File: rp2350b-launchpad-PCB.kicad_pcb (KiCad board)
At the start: 2 copper layers, 58.4 x 83.8 mm, 127 parts, among them J1 Target Isolation Jumpers, J10 PWR Header, J11 LP Extension Heder, J12 LP Header right, J13 PWR Header, J2 Jumper, J3 LiPo 3,7V Batt., J4 Jumper, J5 DBG_PRGM, J6 UART_DBG, J7 DGB Exp. Header, J8 Jumper, J9 LP Header left, SW1 Switch_SP3T, SW2 RESET, SW3 BOOT, U1 MCP73831, U10 WS2812B-2020, U11 WS2812B-2020, U12 WS2812B-2020, U13 WS2812B-2020, U14 WS2812B-2020, U15 WS2812B-2020, U16 WS2812B-2020, U2 XC9142B50C, U3 XC6220B33, U4 25Q32, U5 RP2040, U6 25Q64, U7 APS6404L-3SQR, U8 RP2350_80QFN, U9 WS2812B-2020, Y1 12MHz, Y2 12MHz

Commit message: Footprint cleanup.
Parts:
- U5: footprint rp2350b-launchpad-PCB:QFN40P700X700X90-57N -> Package_DFN_QFN:QFN-56-1EP_7x7mm_P0.4mm_EP3.2x3.2mm_ThermalVias
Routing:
- net GND_DBG: vias 54 -> 52

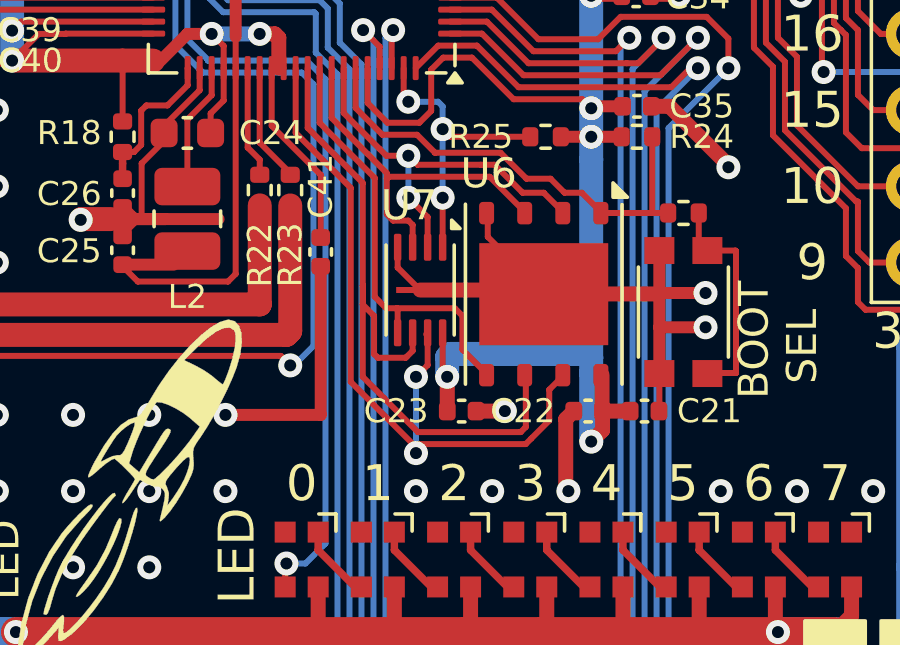
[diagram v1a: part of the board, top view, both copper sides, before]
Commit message: Fixed gerber file names.
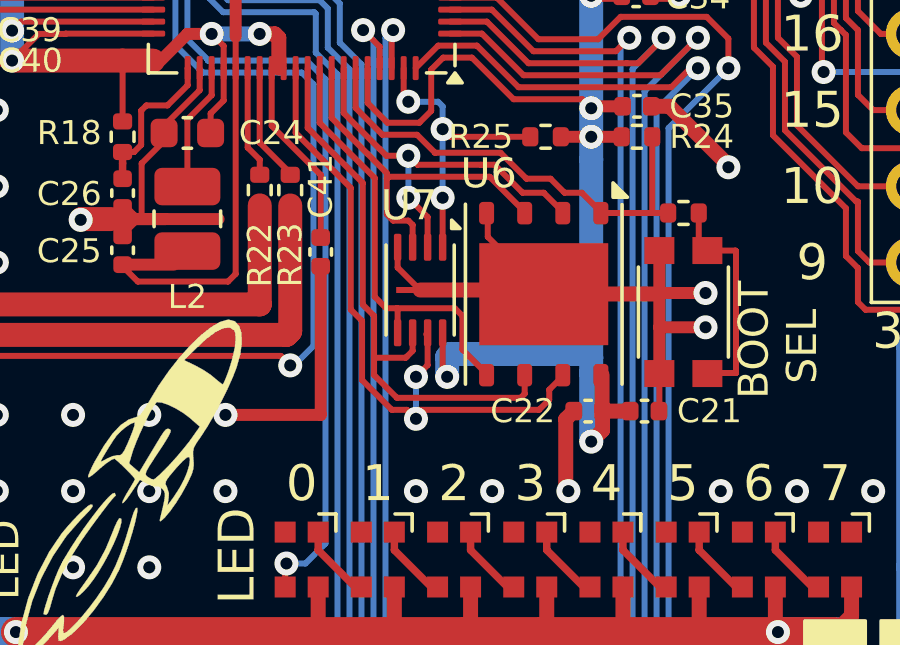
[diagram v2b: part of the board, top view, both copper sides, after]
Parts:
- removed C23: 100nF, Capacitor_SMD:C_0402_1005Metric
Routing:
- net /Target/SCLK: track 23.5 -> 19.1 mm
- net /Target/SD3: track 25.5 -> 22.6 mm
- net +3V3: track 318.8 -> 317.6 mm
- net GND: track 94.1 -> 93.1 mm, vias 98 -> 97
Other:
- rule pad_to_mask_clearance: 0.051 -> 0

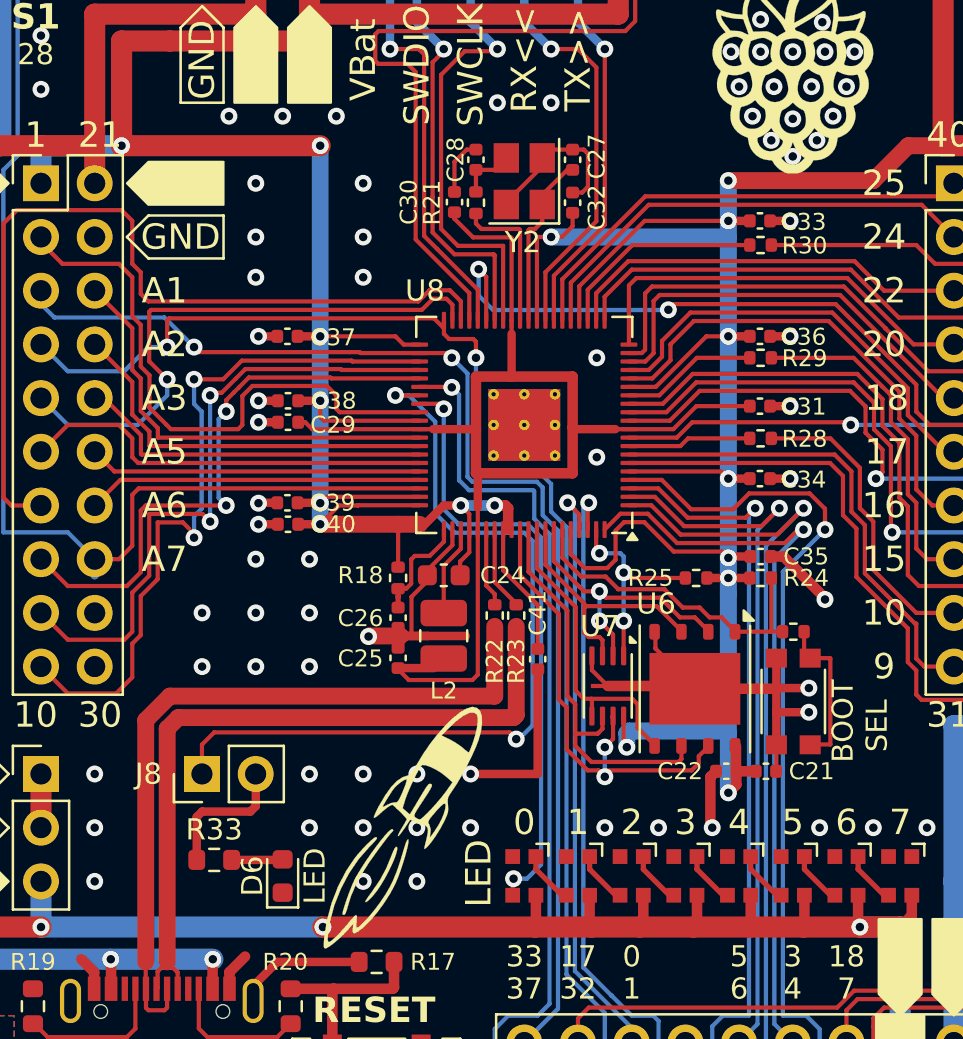
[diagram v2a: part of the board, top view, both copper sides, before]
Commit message: Renumbering parts on target.
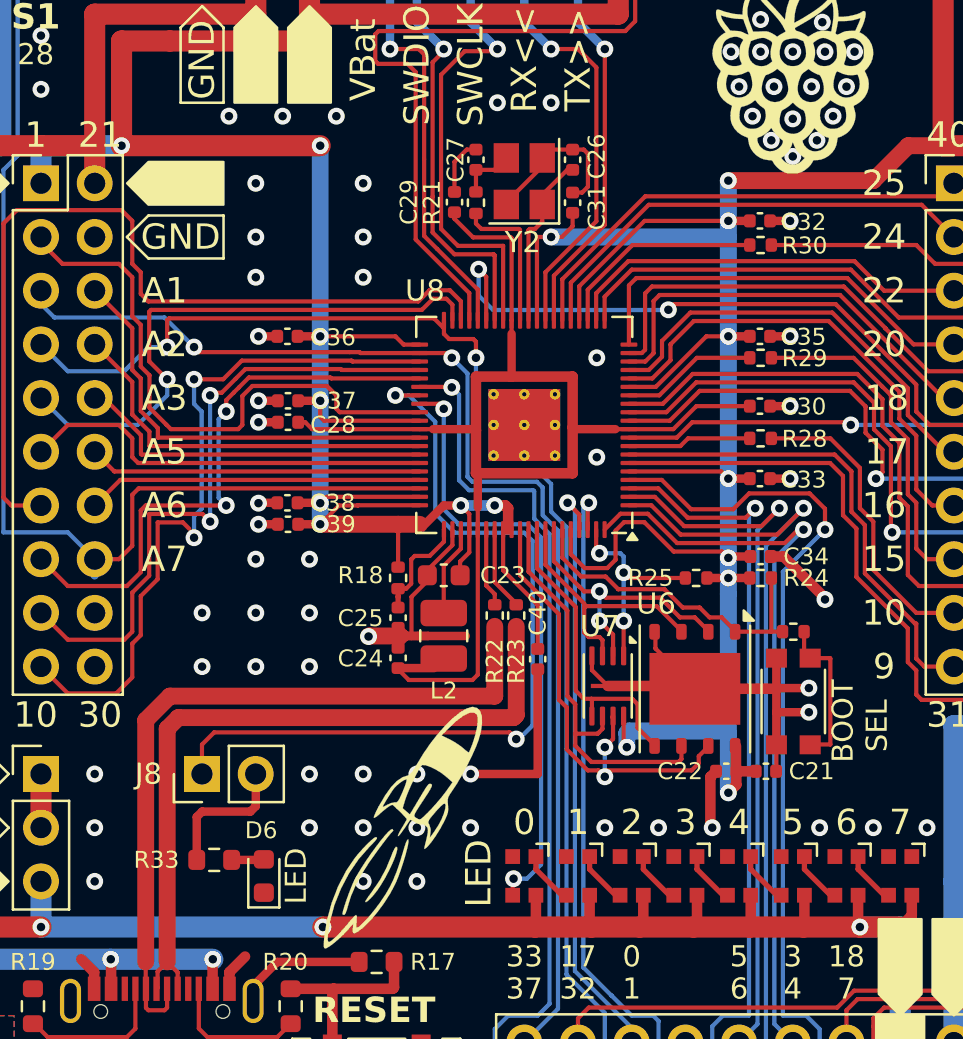
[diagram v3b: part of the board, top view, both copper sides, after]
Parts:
- moved D6 0.89 mm to (127.4, 139.4)
- renumbered C24 to C23, C25 to C24, C26 to C25, C27 to C26, C28 to C27, C29 to C28, C30 to C29, C31 to C30, C32 to C31, C33 to C32, C34 to C33, C35 to C34, C36 to C35, C37 to C36, C38 to C37, C39 to C38, C40 to C39, C41 to C40
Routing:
- net Net-(D6-A): track 2.49 -> 1.53 mm
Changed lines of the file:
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@@
 	(net 10 "Net-(U8-VREG_AVDD)")
 	(net 11 "Net-(U8-XIN)")
-	(net 12 "Net-(C28-Pad2)")
+	(net 12 "Net-(C27-Pad2)")
 	(net 13 "+1V1")
 	(net 14 "Net-(D1-K)")
@@
 		(descr "Capacitor SMD 0603 (1608 Metric), square (rectangular) end terminal, IPC_7351 nominal, (Body size source: IPC-SM-782 page 76, https://www.pcb-3d.com/wordpress/wp-content/uploads/ipc-sm-782a_amendment_1_and_2.pdf), generated with kicad-footprint-generator")
 		(tags "capacitor")
-		(property "Reference" "C24"
+		(property "Reference" "C23"
 			(at 2.794 0 0)
 			(layer "F.SilkS")
@@
 		(descr "Capacitor SMD 0402 (1005 Metric), square (rectangular) end terminal, IPC_7351 nominal, (Body size source: IPC-SM-782 page 76, https://www.pcb-3d.com/wordpress/wp-content/uploads/ipc-sm-782a_amendment_1_and_2.pdf), generated with kicad-footprint-generator")
 		(tags "capacitor")
-		(property "Reference" "C34"
+		(property "Reference" "C33"
 			(at 2.06 0.0508 0)
 			(layer "F.SilkS")
@@
 		(descr "Capacitor SMD 0402 (1005 Metric), square (rectangular) end terminal, IPC_7351 nominal, (Body size source: IPC-SM-782 page 76, https://www.pcb-3d.com/wordpress/wp-content/uploads/ipc-sm-782a_amendment_1_and_2.pdf), generated with kicad-footprint-generator")
 		(tags "capacitor")
-		(property "Reference" "C37"
+		(property "Reference" "C36"
 			(at -2.1564 -0.0508 180)
 			(layer "F.SilkS")
@@
 		(descr "Capacitor SMD 0402 (1005 Metric), square (rectangular) end terminal, IPC_7351 nominal, (Body size source: IPC-SM-782 page 76, https://www.pcb-3d.com/wordpress/wp-content/uploads/ipc-sm-782a_amendment_1_and_2.pdf), generated with kicad-footprint-generator")
 		(tags "capacitor")
-		(property "Reference" "C39"
+		(property "Reference" "C38"
 			(at -2.131 0 180)
 			(layer "F.SilkS")
@@
 		(descr "Capacitor SMD 0402 (1005 Metric), square (rectangular) end terminal, IPC_7351 nominal, (Body size source: IPC-SM-782 page 76, https://www.pcb-3d.com/wordpress/wp-content/uploads/ipc-sm-782a_amendment_1_and_2.pdf), generated with kicad-footprint-generator")
 		(tags "capacitor")
-		(property "Reference" "C26"
+		(property "Reference" "C25"
 			(at -1.877 1.778 0)
 			(layer "F.SilkS")
@@
 		(descr "Capacitor SMD 0402 (1005 Metric), square (rectangular) end terminal, IPC_7351 nominal, (Body size source: IPC-SM-782 page 76, https://www.pcb-3d.com/wordpress/wp-content/uploads/ipc-sm-782a_amendment_1_and_2.pdf), generated with kicad-footprint-generator")
 		(tags "capacitor")
-		(property "Reference" "C30"
+		(property "Reference" "C29"
 			(at 0 -2.159 90)
 			(layer "F.SilkS")
@@
 		(descr "Capacitor SMD 0402 (1005 Metric), square (rectangular) end terminal, IPC_7351 nominal, (Body size source: IPC-SM-782 page 76, https://www.pcb-3d.com/wordpress/wp-content/uploads/ipc-sm-782a_amendment_1_and_2.pdf), generated with kicad-footprint-generator")
 		(tags "capacitor")
-		(property "Reference" "C31"
+		(property "Reference" "C30"
 			(at 2.06 0.0254 0)
 			(layer "F.SilkS")
@@
 		(descr "Capacitor SMD 0402 (1005 Metric), square (rectangular) end terminal, IPC_7351 nominal, (Body size source: IPC-SM-782 page 76, https://www.pcb-3d.com/wordpress/wp-content/uploads/ipc-sm-782a_amendment_1_and_2.pdf), generated with kicad-footprint-generator")
 		(tags "capacitor")
-		(property "Reference" "C28"
+		(property "Reference" "C27"
 			(at 0 0.962 90)
 			(layer "F.SilkS")
@@
 			(layers "F.Cu" "F.Paste" "F.Mask")
 			(roundrect_rratio 0.25)
-			(net 12 "Net-(C28-Pad2)")
+			(net 12 "Net-(C27-Pad2)")
 			(pintype "passive")
 		)
@@
 		(descr "Capacitor SMD 0402 (1005 Metric), square (rectangular) end terminal, IPC_7351 nominal, (Body size source: IPC-SM-782 page 76, https://www.pcb-3d.com/wordpress/wp-content/uploads/ipc-sm-782a_amendment_1_and_2.pdf), generated with kicad-footprint-generator")
 		(tags "capacitor")
-		(property "Reference" "C41"
+		(property "Reference" "C40"
 			(at -2.187 0 90)
 			(layer "F.SilkS")
@@
 		(tags "resistor")
 		(property "Reference" "R33"
-			(at 0 -1.43 0)
+			(at -2.731 0 0)
 			(layer "F.SilkS")
 			(effects
 				(font
-					(size 1 1)
+					(size 0.8 0.8)
 					(thickness 0.15)
 				)
@@
 			(layers "F.Cu" "F.Paste" "F.Mask")
 			(roundrect_rratio 0.25)
-			(net 12 "Net-(C28-Pad2)")
+			(net 12 "Net-(C27-Pad2)")
 			(pintype "passive")
 		)
@@
 		(descr "Capacitor SMD 0402 (1005 Metric), square (rectangular) end terminal, IPC_7351 nominal, (Body size source: IPC-SM-782 page 76, https://www.pcb-3d.com/wordpress/wp-content/uploads/ipc-sm-782a_amendment_1_and_2.pdf), generated with kicad-footprint-generator")
 		(tags "capacitor")
-		(property "Reference" "C38"
+		(property "Reference" "C37"
 			(at -2.159 0 180)
 			(layer "F.SilkS")
@@
 		(descr "Capacitor SMD 0402 (1005 Metric), square (rectangular) end terminal, IPC_7351 nominal, (Body size source: IPC-SM-782 page 76, https://www.pcb-3d.com/wordpress/wp-content/uploads/ipc-sm-782a_amendment_1_and_2.pdf), generated with kicad-footprint-generator")
 		(tags "capacitor")
-		(property "Reference" "C33"
+		(property "Reference" "C32"
 			(at 2.06 0.054 0)
 			(layer "F.SilkS")
@@
 		(descr "Capacitor SMD 0402 (1005 Metric), square (rectangular) end terminal, IPC_7351 nominal, (Body size source: IPC-SM-782 page 76, https://www.pcb-3d.com/wordpress/wp-content/uploads/ipc-sm-782a_amendment_1_and_2.pdf), generated with kicad-footprint-generator")
 		(tags "capacitor")
-		(property "Reference" "C25"
+		(property "Reference" "C24"
 			(at 1.933 1.778 180)
 			(layer "F.SilkS")
@@
 		(descr "Capacitor SMD 0402 (1005 Metric), square (rectangular) end terminal, IPC_7351 nominal, (Body size source: IPC-SM-782 page 76, https://www.pcb-3d.com/wordpress/wp-content/uploads/ipc-sm-782a_amendment_1_and_2.pdf), generated with kicad-footprint-generator")
 		(tags "capacitor")
-		(property "Reference" "C27"
+		(property "Reference" "C26"
 			(at -0.155 -1.143 90)
 			(layer "F.SilkS")
@@
 	(footprint "LED_SMD:LED_0603_1608Metric"
 		(layer "F.Cu")
-		(at 128.27 139.446 90)
+		(at 127.381 139.446 90)
 		(descr "LED SMD 0603 (1608 Metric), square (rectangular) end terminal, IPC_7351 nominal, (Body size source: http://www.tortai-tech.com/upload/download/2011102023233369053.pdf), generated with kicad-footprint-generator")
 		(tags "LED")
 		(property "Reference" "D6"
-			(at 0 -1.43 90)
+			(at 2.159 -0.127 180)
 			(layer "F.SilkS")
 			(effects
 				(font
-					(size 1 1)
+					(size 0.8 0.8)
 					(thickness 0.15)
 				)
@@
 		(descr "Capacitor SMD 0402 (1005 Metric), square (rectangular) end terminal, IPC_7351 nominal, (Body size source: IPC-SM-782 page 76, https://www.pcb-3d.com/wordpress/wp-content/uploads/ipc-sm-782a_amendment_1_and_2.pdf), generated with kicad-footprint-generator")
 		(tags "capacitor")
-		(property "Reference" "C29"
+		(property "Reference" "C28"
 			(at -2.131 -0.127 0)
 			(layer "F.SilkS")
@@
 		(descr "Capacitor SMD 0402 (1005 Metric), square (rectangular) end terminal, IPC_7351 nominal, (Body size source: IPC-SM-782 page 76, https://www.pcb-3d.com/wordpress/wp-content/uploads/ipc-sm-782a_amendment_1_and_2.pdf), generated with kicad-footprint-generator")
 		(tags "capacitor")
-		(property "Reference" "C32"
+		(property "Reference" "C31"
 			(at -0.226 1.143 90)
 			(layer "F.SilkS")
@@
 		(descr "Capacitor SMD 0402 (1005 Metric), square (rectangular) end terminal, IPC_7351 nominal, (Body size source: IPC-SM-782 page 76, https://www.pcb-3d.com/wordpress/wp-content/uploads/ipc-sm-782a_amendment_1_and_2.pdf), generated with kicad-footprint-generator")
 		(tags "capacitor")
-		(property "Reference" "C36"
+		(property "Reference" "C35"
 			(at 2.06 0.0254 0)
 			(layer "F.SilkS")
@@
 		(descr "Capacitor SMD 0402 (1005 Metric), square (rectangular) end terminal, IPC_7351 nominal, (Body size source: IPC-SM-782 page 76, https://www.pcb-3d.com/wordpress/wp-content/uploads/ipc-sm-782a_amendment_1_and_2.pdf), generated with kicad-footprint-generator")
 		(tags "capacitor")
-		(property "Reference" "C35"
+		(property "Reference" "C34"
 			(at 2.159 0 0)
 			(layer "F.SilkS")
@@
 			(size 1.4 1.2)
 			(layers "F.Cu" "F.Paste" "F.Mask")
-			(net 12 "Net-(C28-Pad2)")
+			(net 12 "Net-(C27-Pad2)")
 			(pinfunction "3")
 			(pintype "passive")
@@
 		(descr "Capacitor SMD 0402 (1005 Metric), square (rectangular) end terminal, IPC_7351 nominal, (Body size source: IPC-SM-782 page 76, https://www.pcb-3d.com/wordpress/wp-content/uploads/ipc-sm-782a_amendment_1_and_2.pdf), generated with kicad-footprint-generator")
 		(tags "capacitor")
-		(property "Reference" "C40"
+		(property "Reference" "C39"
 			(at -2.131 0 180)
 			(layer "F.SilkS")
@@
 	)
 	(segment
-		(start 125.781 138.684)
-		(end 128.27 138.684)
+		(start 127.3555 138.684)
+		(end 127.381 138.6585)
+		(width 0.4)
+		(layer "F.Cu")
+		(net 151)
+	)
+	(segment
+		(start 125.857 138.684)
+		(end 127.3555 138.684)
 		(width 0.4)
 		(layer "F.Cu")
